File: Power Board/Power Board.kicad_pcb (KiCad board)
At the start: 4 copper layers, 211 parts, among them IC1 LTC4151IMS#PBF, IC2 LTC4151IMS#PBF, J1 Conn_01x02, J10 Conn_01x02, J11 Conn_01x02, J12 Conn_01x02, J13 Conn_01x02, J14 Conn_01x02, J15 Conn_01x02, J16 Conn_01x02, J17 Conn_01x02, J18 Conn_02x03_Top_Bottom, J2 Conn_01x02, J20 Conn_02x03_Top_Bottom, J3 Conn_01x02, J4 Conn_01x02, J5 Conn_01x02, J6 Conn_01x02, J7 Conn_01x02, J8 Conn_01x02, J9 Conn_02x03_Top_Bottom, Q1 Q_PMOS_GDS, Q10 Q_NMOS_GDS, Q11 Q_NMOS_GDS, Q12 Q_NMOS_GDS, Q13 Q_NMOS_GDS, Q14 Q_NMOS_GDS, Q15 Q_NMOS_GDS, Q16 Q_NMOS_GDS, Q17 Q_NMOS_GDS, Q18 Q_NMOS_GDS, Q19 Q_NMOS_GDS, Q2 Q_PMOS_GDS, Q20 Q_NMOS_GDS, Q21 Q_NMOS_GDS, Q22 Q_NMOS_GDS, Q3 Q_PMOS_GDS, Q4 Q_PMOS_GDS, Q5 Q_PMOS_GDS, Q6 Q_PMOS_GDS, Q7 Q_PMOS_GDS, Q8 Q_PMOS_GDS, Q9 Q_NMOS_GDS, U1 LTC4372CDD-PBF, U10 ACS770xCB-050U-PFF, U11 ACS770xCB-050U-PFF, U12 ACS770xCB-050U-PFF, U13 ACS770xCB-050U-PFF, U14 ACS770xCB-050U-PFF, U15 ADC128S052CIMT, U16 ADC128S052CIMT, U17 TLV70033_SOT23-5, U2 LTC4372CDD-PBF, U3 LTC4372CDD-PBF, U4 LTC4372CDD-PBF, U5 LTC4372CDD-PBF, U6 LTC4372CDD-PBF, U7 LTC4372CDD-PBF, U8 ACS770xCB-050U-PFF, U9 ACS770xCB-050U-PFF

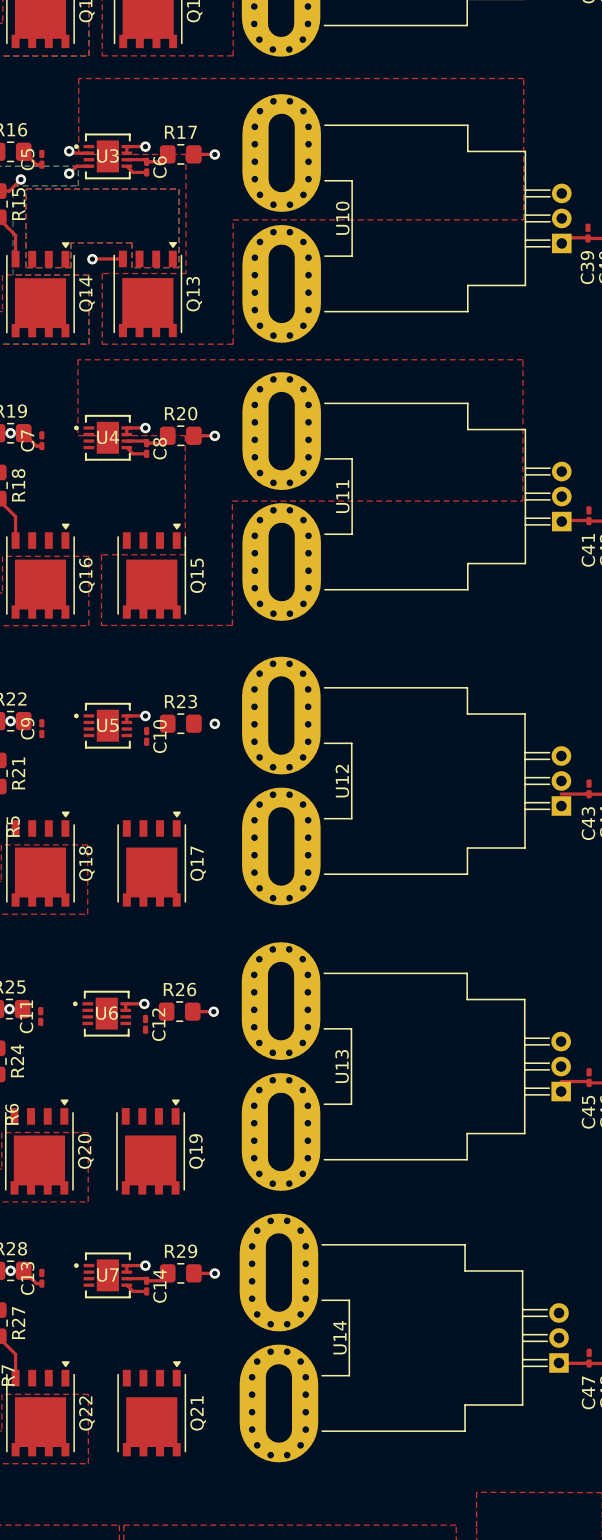
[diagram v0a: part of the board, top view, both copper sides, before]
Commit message: pours battery presense
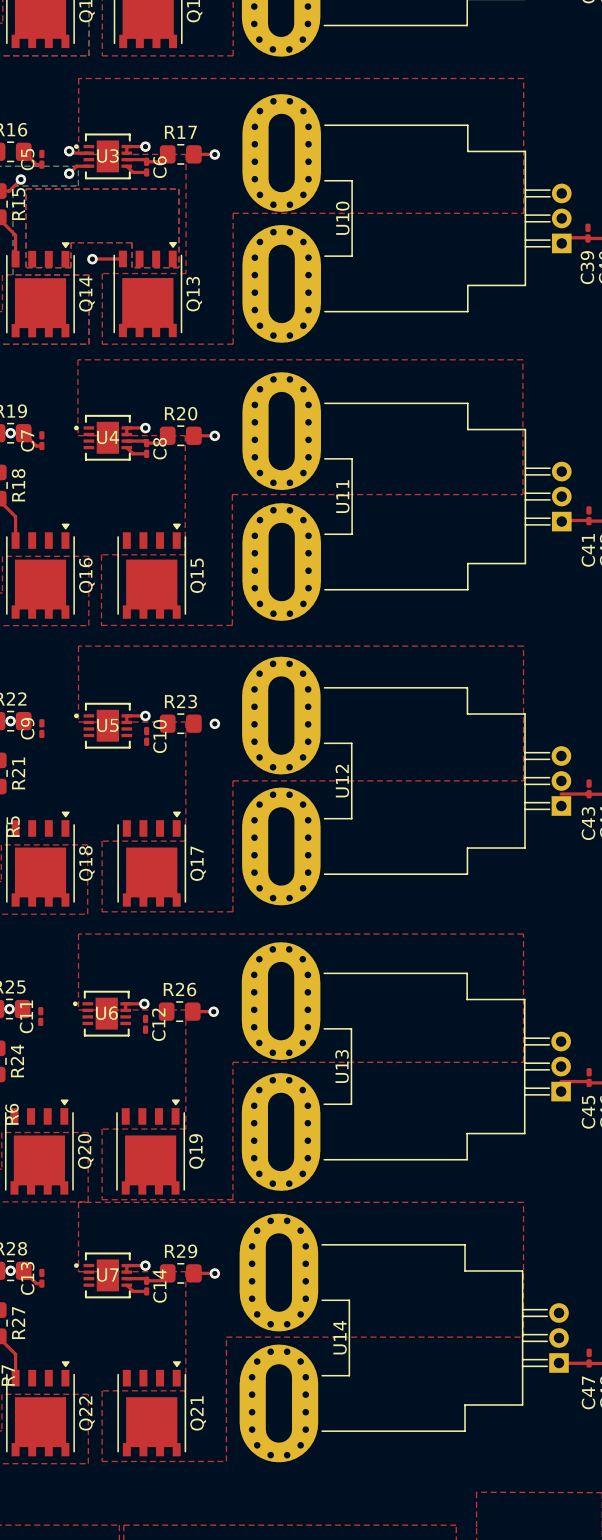
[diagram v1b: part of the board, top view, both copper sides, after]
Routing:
- added copper zone on F.Cu, net /BATT_5_PRESENSE
- added copper zone on F.Cu, net /BATT_6_PRESENSE
- added copper zone on F.Cu, net /BATT_7_PRESENSE
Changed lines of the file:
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@@
 		(polygon
 			(pts
-				(xy 120.4 86.631626) (xy 120.4 92.031626) (xy 130.4 92.031626) (xy 130.4 82.531626) (xy 152.6 82.531626)
+				(xy 120.4 86.631626) (xy 120.4 92.031626) (xy 130.4 92.031626) (xy 130.4 82.031626) (xy 152.6 82.031626)
 				(xy 152.6 71.731626) (xy 118.6 71.731626) (xy 118.6 77.531626) (xy 119.8 77.531626) (xy 126.8 77.531626)
 				(xy 126.8 86.631626)
@@
 	)
 	(zone
+		(net 89)
+		(net_name "/BATT_7_PRESENSE")
+		(layer "F.Cu")
+		(hatch full 0.5)
+		(priority 10)
+		(connect_pads yes
+			(clearance 0.5)
+		)
+		(min_thickness 0.25)
+		(filled_areas_thickness no)
+		(fill yes
+			(thermal_gap 0.5)
+			(thermal_bridge_width 0.5)
+		)
+		(polygon
+			(pts
+				(xy 120.385 172) (xy 120.385 177.4) (xy 129.885 177.4) (xy 129.885 167.9) (xy 152.585 167.9) (xy 152.585 157.6)
+				(xy 118.585 157.6) (xy 118.585 162.9) (xy 119.785 162.9) (xy 126.785 162.9) (xy 126.785 172)
+			)
+		)
+	)
+	(zone
 		(net 100)
 		(net_name "/BATT_1")
@@
 	)
 	(zone
+		(net 88)
+		(net_name "/BATT_6_PRESENSE")
+		(layer "F.Cu")
+		(hatch full 0.5)
+		(priority 10)
+		(connect_pads yes
+			(clearance 0.5)
+		)
+		(min_thickness 0.25)
+		(filled_areas_thickness no)
+		(fill yes
+			(thermal_gap 0.5)
+			(thermal_bridge_width 0.5)
+		)
+		(polygon
+			(pts
+				(xy 120.385 152) (xy 120.385 157.4) (xy 130.385 157.4) (xy 130.385 146.9) (xy 152.585 146.9) (xy 152.585 137.1)
+				(xy 118.585 137.1) (xy 118.585 142.9) (xy 119.785 142.9) (xy 126.785 142.9) (xy 126.785 152)
+			)
+		)
+	)
+	(zone
 		(net 20)
 		(net_name "/24V_UNREGULATED")
@@
 		(polygon
 			(pts
-				(xy 120.34084 108.11942) (xy 120.34084 113.51942) (xy 130.34084 113.51942) (xy 130.34084 104.01942)
-				(xy 152.54084 104.01942) (xy 152.54084 93.21942) (xy 118.54084 93.21942) (xy 118.54084 99.01942)
+				(xy 120.34084 108.11942) (xy 120.34084 113.51942) (xy 130.34084 113.51942) (xy 130.34084 103.51942)
+				(xy 152.54084 103.51942) (xy 152.54084 93.21942) (xy 118.54084 93.21942) (xy 118.54084 99.01942)
 				(xy 119.74084 99.01942) (xy 126.74084 99.01942) (xy 126.74084 108.11942)
 			)
@@
 			)
 		)
+	)
+	(zone
+		(net 87)
+		(net_name "/BATT_5_PRESENSE")
+		(layer "F.Cu")
+		(hatch full 0.5)
+		(priority 10)
+		(connect_pads yes
+			(clearance 0.5)
+		)
+		(min_thickness 0.25)
+		(filled_areas_thickness no)
+		(fill yes
+			(thermal_gap 0.5)
+			(thermal_bridge_width 0.5)
+		)
+		(polygon
+			(pts
+				(xy 120.385 130) (xy 120.385 135.4) (xy 130.385 135.4) (xy 130.385 125.4) (xy 152.585 125.4) (xy 152.585 115.1)
+				(xy 118.585 115.1) (xy 118.585 120.9) (xy 119.785 120.9) (xy 126.785 120.9) (xy 126.785 130)
+			)
+		)

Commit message: pours battery
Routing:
- added copper zone on F.Cu, net /BATT_2
- added copper zone on F.Cu, net /BATT_3
- added copper zone on F.Cu, net /BATT_4
- added copper zone on F.Cu, net /BATT_5
- added copper zone on F.Cu, net /BATT_6
- added copper zone on F.Cu, net /BATT_7
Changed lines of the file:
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@@
+	)
+	(zone
+		(net 102)
+		(net_name "/BATT_3")
+		(layer "F.Cu")
+		(hatch full 0.5)
+		(priority 7)
+		(connect_pads
+			(clearance 0.5)
+		)
+		(min_thickness 0.25)
+		(filled_areas_thickness no)
+		(fill yes
+			(thermal_gap 0.5)
+			(thermal_bridge_width 0.5)
+		)
+		(polygon
+			(pts
+				(xy 130.985 82.85) (xy 152.585 82.85) (xy 152.585 92.6) (xy 130.985 92.6)
+			)
+		)
 	)
 	(zone
@@
 	)
 	(zone
+		(net 104)
+		(net_name "/BATT_5")
+		(layer "F.Cu")
+		(hatch full 0.5)
+		(priority 7)
+		(connect_pads
+			(clearance 0.5)
+		)
+		(min_thickness 0.25)
+		(filled_areas_thickness no)
+		(fill yes
+			(thermal_gap 0.5)
+			(thermal_bridge_width 0.5)
+		)
+		(polygon
+			(pts
+				(xy 130.985 125.85) (xy 152.585 125.85) (xy 152.585 135.6) (xy 130.985 135.6)
+			)
+		)
+	)
+	(zone
 		(net 19)
 		(net_name "GND")
@@
 	)
 	(zone
+		(net 101)
+		(net_name "/BATT_2")
+		(layer "F.Cu")
+		(hatch full 0.5)
+		(priority 7)
+		(connect_pads
+			(clearance 0.5)
+		)
+		(min_thickness 0.25)
+		(filled_areas_thickness no)
+		(fill yes
+			(thermal_gap 0.5)
+			(thermal_bridge_width 0.5)
+		)
+		(polygon
+			(pts
+				(xy 131 60.85) (xy 152.6 60.85) (xy 152.6 70.6) (xy 131 70.6)
+			)
+		)
+	)
+	(zone
+		(net 105)
+		(net_name "/BATT_6")
+		(layer "F.Cu")
+		(hatch full 0.5)
+		(priority 7)
+		(connect_pads
+			(clearance 0.5)
+		)
+		(min_thickness 0.25)
+		(filled_areas_thickness no)
+		(fill yes
+			(thermal_gap 0.5)
+			(thermal_bridge_width 0.5)
+		)
+		(polygon
+			(pts
+				(xy 130.985 147.35) (xy 152.585 147.35) (xy 152.585 157.1) (xy 130.985 157.1)
+			)
+		)
+	)
+	(zone
+		(net 103)
+		(net_name "/BATT_4")
+		(layer "F.Cu")
+		(hatch full 0.5)
+		(priority 7)
+		(connect_pads
+			(clearance 0.5)
+		)
+		(min_thickness 0.25)
+		(filled_areas_thickness no)
+		(fill yes
+			(thermal_gap 0.5)
+			(thermal_bridge_width 0.5)
+		)
+		(polygon
+			(pts
+				(xy 130.985 103.85) (xy 152.585 103.85) (xy 152.585 113.6) (xy 130.985 113.6)
+			)
+		)
+	)
+	(zone
 		(net 19)
 		(net_name "GND")
@@
 			)
 		)
+	)
+	(zone
+		(net 106)
+		(net_name "/BATT_7")
+		(layer "F.Cu")
+		(hatch full 0.5)
+		(priority 7)
+		(connect_pads
+			(clearance 0.5)
+		)
+		(min_thickness 0.25)
+		(filled_areas_thickness no)
+		(fill yes
+			(thermal_gap 0.5)
+			(thermal_bridge_width 0.5)
+		)
+		(polygon
+			(pts
+				(xy 130.985 168.35) (xy 152.585 168.35) (xy 152.585 178.1) (xy 130.985 178.1)
+			)
+		)

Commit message: pours battery
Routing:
- net Net-(Q21-S): vias 0 -> 5
- net Net-(Q19-S): vias 0 -> 5
- net Net-(Q17-S): vias 0 -> 5
- net Net-(Q15-S): vias 0 -> 5
- net Net-(Q13-S): vias 0 -> 5
- added copper zone on B.Cu, net /BATT_2
- added copper zone on B.Cu, net /BATT_2_PRESENSE
- added copper zone on B.Cu, net /BATT_3
- added copper zone on B.Cu, net /BATT_3_PRESENSE
- added copper zone on B.Cu, net /BATT_4
- added copper zone on B.Cu, net /BATT_4_PRESENSE
- added copper zone on B.Cu, net /BATT_5
- added copper zone on B.Cu, net /BATT_5_PRESENSE
- added copper zone on B.Cu, net /BATT_6
- added copper zone on B.Cu, net /BATT_6_PRESENSE
- added copper zone on B.Cu, net /BATT_7
- added copper zone on B.Cu, net /BATT_7_PRESENSE
- added copper zone on B.Cu, net /BATT_IN_12_4
- added copper zone on B.Cu, net /BATT_IN_12_5
- added copper zone on B.Cu, net /BATT_IN_12_6
- added copper zone on B.Cu, net /BATT_IN_12_7
- added copper zone on B.Cu, net Net-(Q15-S)
- added copper zone on F.Cu, net Net-(Q15-S)
- added copper zone on B.Cu, net Net-(Q17-S)
- added copper zone on F.Cu, net Net-(Q17-S)
- added copper zone on B.Cu, net Net-(Q19-S)
- added copper zone on F.Cu, net Net-(Q19-S)
- added copper zone on B.Cu, net Net-(Q21-S)
- added copper zone on F.Cu, net Net-(Q21-S)

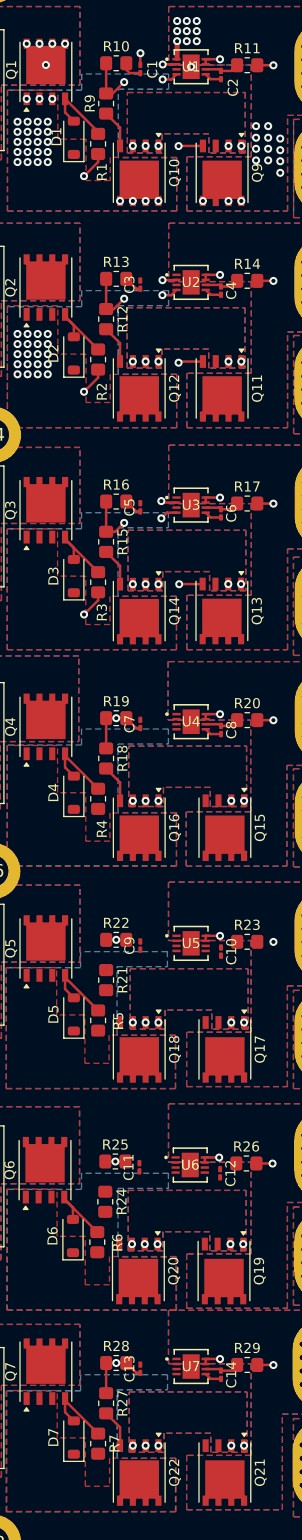
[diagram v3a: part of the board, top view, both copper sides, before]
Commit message: minor tracing updates for batteries on PDB
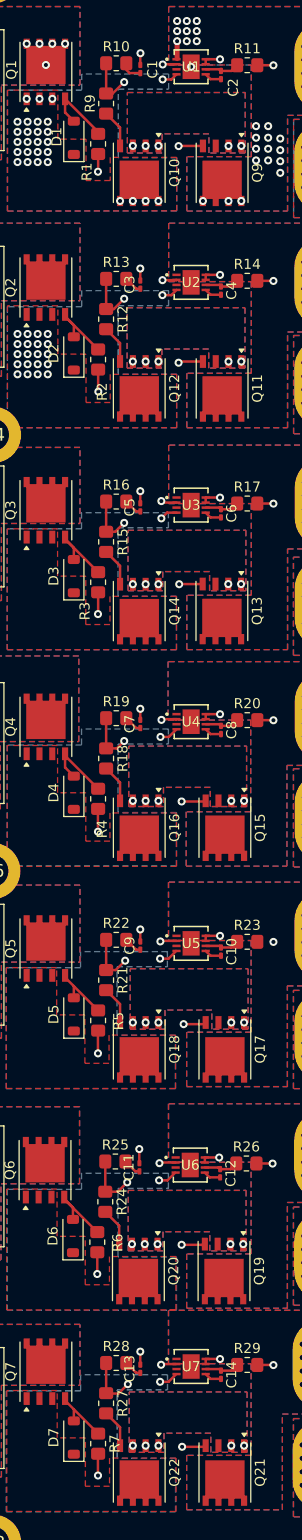
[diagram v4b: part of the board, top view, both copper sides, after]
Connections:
- U6 pad 1: unconnected-(U6-OUT-Pad1) -> /BATT_6_PRESENSE
- U6 pad 2: unconnected-(U6-GATE-Pad2) -> Net-(Q19-G)
- U6 pad 3: unconnected-(U6-SOURCE-Pad3) -> Net-(Q19-S)
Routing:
- net Net-(Q17-G): track 0.00 -> 22.2 mm, vias 0 -> 3
- net Net-(Q19-G): track 0.00 -> 22.1 mm, vias 0 -> 3
- net Net-(Q21-G): track 3.00 -> 22.1 mm, vias 0 -> 3
- net Net-(Q15-G): track 3.00 -> 22.0 mm, vias 0 -> 3
- net GND: track 40.2 -> 54.2 mm, vias 31 -> 37
- net Net-(Q20-G): track 0.00 -> 3.78 mm
- net Net-(Q18-G): track 0.00 -> 3.78 mm
- net Net-(C10-Pad1): track 0.00 -> 3.43 mm
- net Net-(C12-Pad1): track 0.00 -> 3.43 mm
- net /BATT_IN_12_6: track 0.00 -> 1.91 mm, vias 0 -> 1
- net /BATT_IN_12_5: track 0.00 -> 1.91 mm, vias 0 -> 1
- net /BATT_IN_12_4: track 0.00 -> 1.91 mm, vias 0 -> 1
- net /BATT_IN_12_7: track 0.00 -> 1.91 mm, vias 0 -> 1
- net Net-(C11-Pad1): track 0.00 -> 1.79 mm
- net Net-(C9-Pad1): track 0.00 -> 1.79 mm
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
